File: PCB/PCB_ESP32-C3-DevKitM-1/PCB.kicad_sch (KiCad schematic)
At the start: 4 parts, among them J1 Conn_01x08_Socket, U1 ESP32-C3-DEVKITM-1

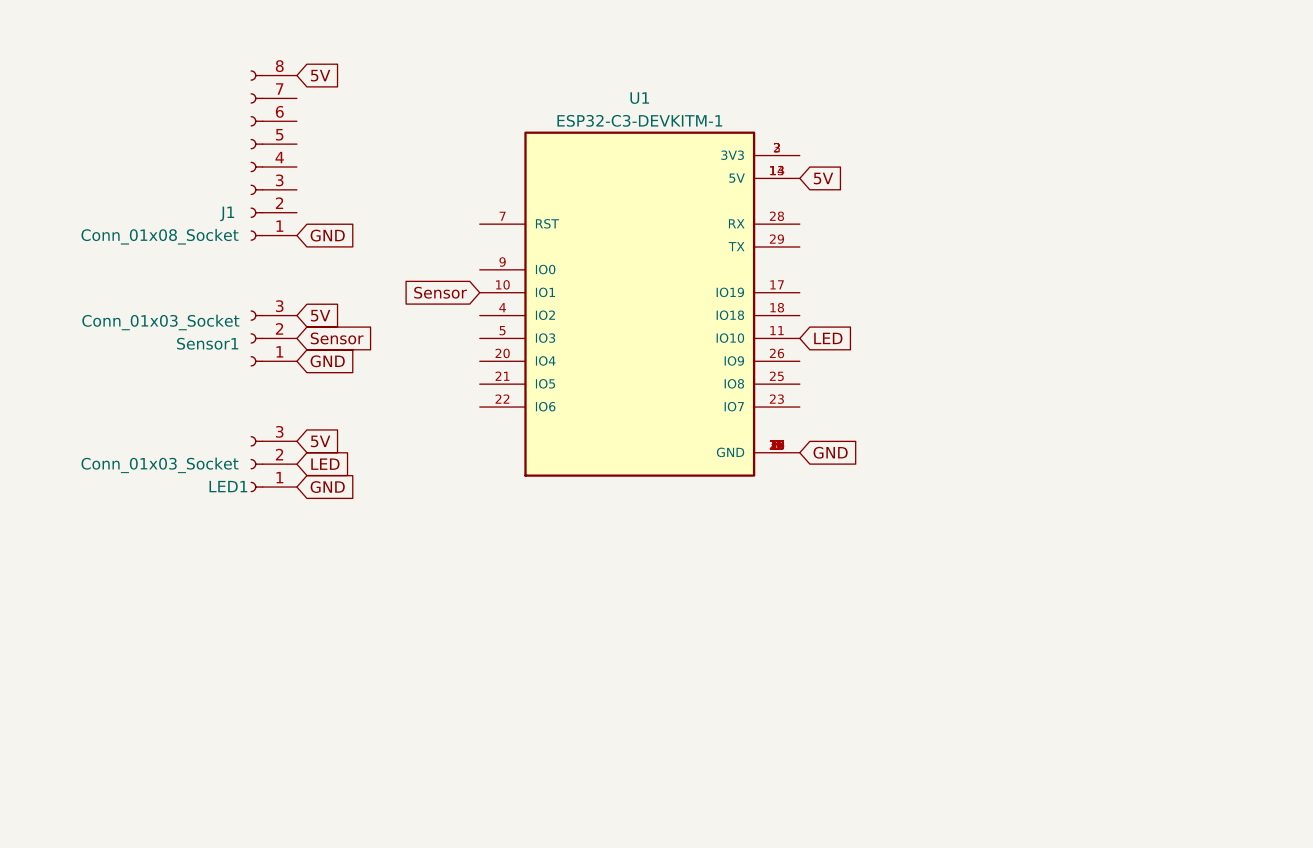
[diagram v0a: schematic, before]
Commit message: adding more pcb versions and a readme with explenation
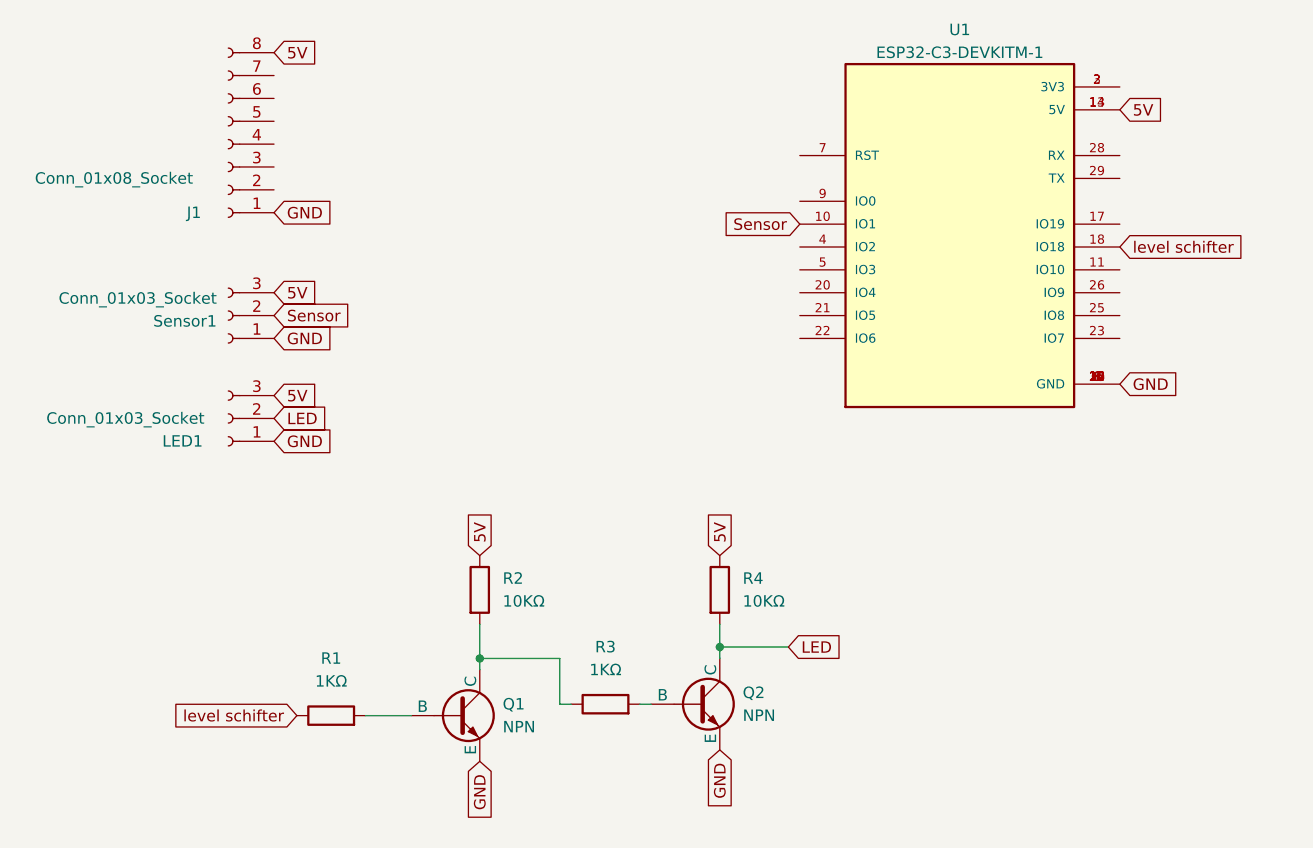
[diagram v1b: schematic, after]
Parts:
- added Q1, Q2: NPN, Package_TO_SOT_SMD:SOT-23, symbol Simulation_SPICE:NPN
- added R1, R3: 1KΩ, Resistor_SMD:R_0805_2012Metric, symbol Device:R
- added R2, R4: 10KΩ, Resistor_SMD:R_0805_2012Metric, symbol Device:R
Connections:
- net 5V: now also R2.1, R4.1
- net GND: now also Q1.3 (E), Q2.3 (E)
- net LED: now also Q2.1 (C), R4.2; no longer U1.11 (IO10)
- net level schifter: now reaches U1.18 (IO18)
- net level schifter: now also R1.1
- new net: Q1.1 (C), R2.2, R3.1
- new net: Q2.2 (B), R3.2
- new net: Q1.2 (B), R1.2
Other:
- moved on the sheet: J1, LED1, Sensor1, U1
